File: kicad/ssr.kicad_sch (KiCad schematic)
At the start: 15 parts, among them J10 ULN spare, J11 SSR G17, J12 SSR G22, J13 SSR G23, J14 SSR G27, U4 ULN2803A

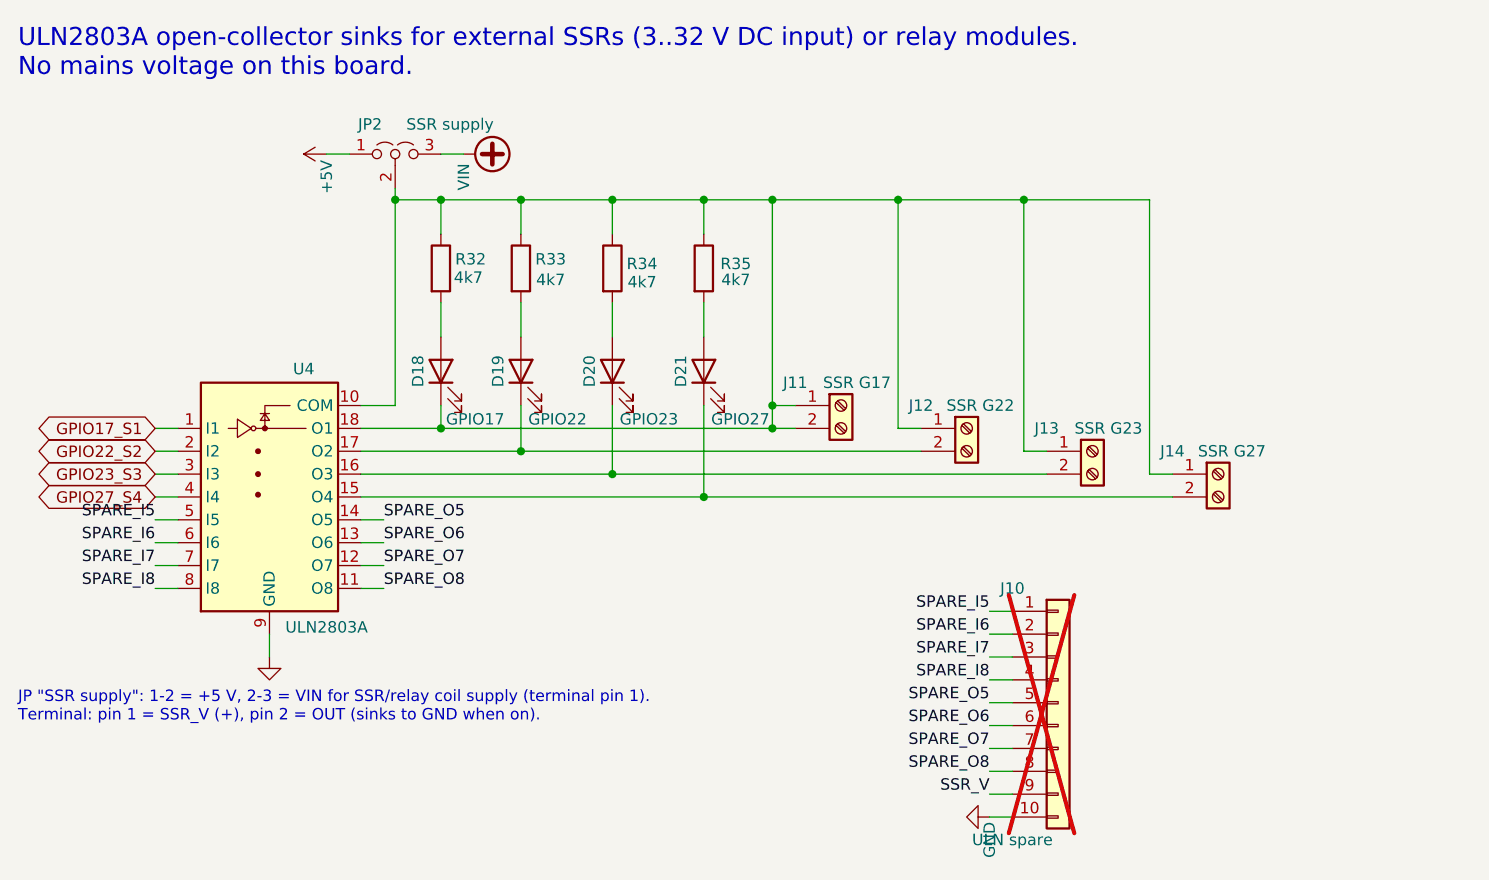
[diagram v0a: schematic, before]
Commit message: kicad: drop J10, fix S1 output shorted to SSR_V
- J10 (ULN2803 spare header) removed from schematic and board; the four
  unused ULN channels (U4 pins 5-8, 11-14) are marked no-connect
- schematic: a wire in front of J11 joined its two stubs, shorting the
  S1 output (U4 O1, D18, J11 pin 2) to SSR_V; removed. The board carried
  the merged net too but no copper joined both sides; pads and tracks
  are split again (SSR side now Net-(J11-Pin_1), S1 side Net-(D18-K))
- dangling 1.27 mm wire at R14 (outputs sheet) removed
ERC 0; DRC with schematic parity: only the known J2/Zero-hole overlap
and unrouted nets. Docs: J10 removed from README/BOM.

Co-Authored-By: Claude Opus 5.5 (1M context) <noreply@anthropic.com>
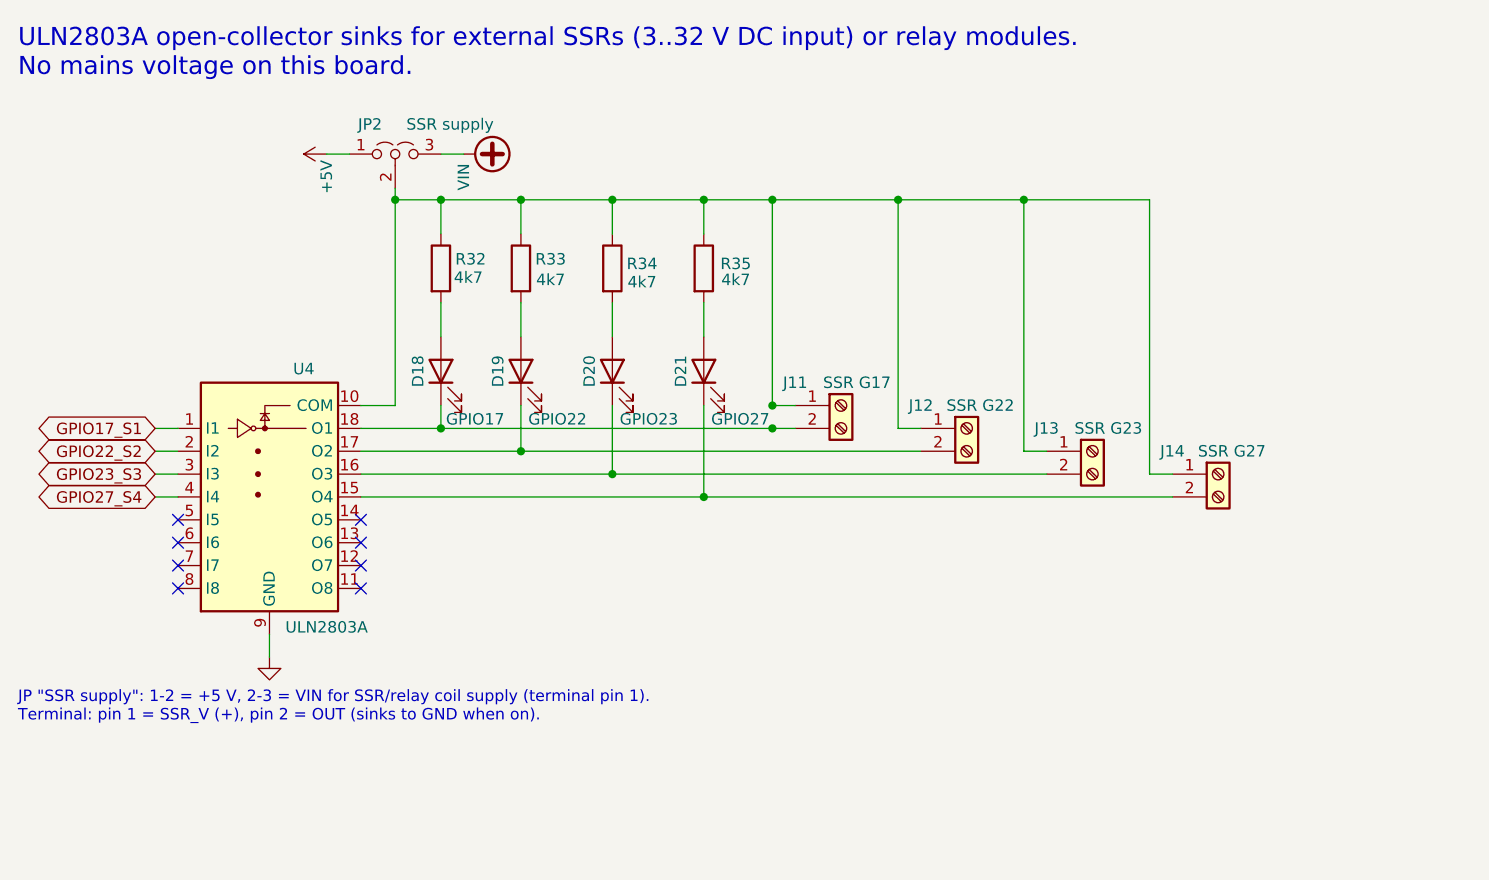
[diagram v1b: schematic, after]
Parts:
- removed J10: ULN spare, Connector_PinHeader_2.54mm:PinHeader_1x10_P2.54mm_Vertical, symbol Connector_Generic:Conn_01x10
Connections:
- net at J11.1 (Pin_1), J12.1 (Pin_1), J13.1 (Pin_1)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: no longer D18.1 (K), J11.2 (Pin_2), U4.18 (O1)
- net SPARE_I5: no longer names the net of U4.5 (I5)
- net SPARE_I6: no longer names the net of U4.6 (I6)
- net SPARE_I7: no longer names the net of U4.7 (I7)
- net SPARE_I8: no longer names the net of U4.8 (I8)
- net SPARE_O5: no longer names the net of U4.14 (O5)
- net SPARE_O6: no longer names the net of U4.13 (O6)
- net SPARE_O7: no longer names the net of U4.12 (O7)
- net SPARE_O8: no longer names the net of U4.11 (O8)
- new net: D18.1 (K), J11.2 (Pin_2), U4.18 (O1)
- no-connect marks 0 -> 8

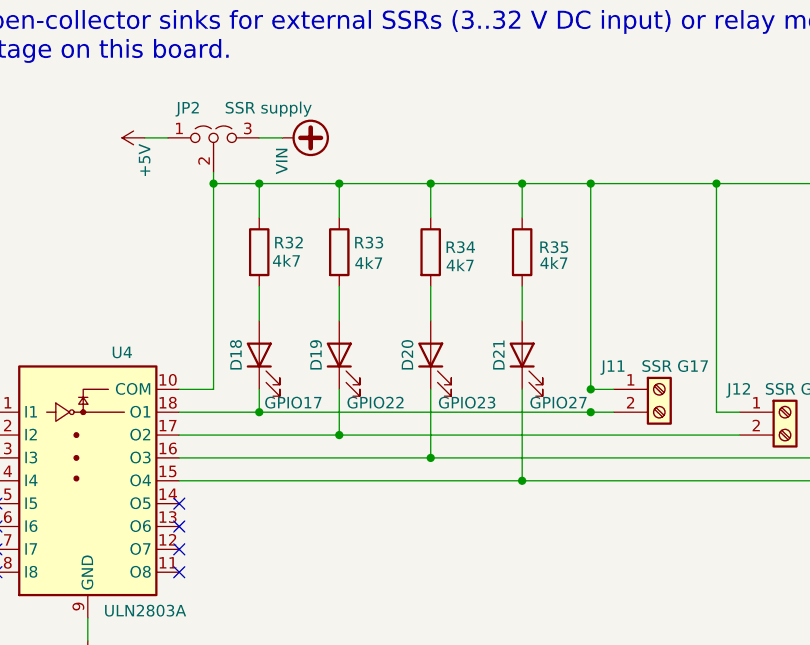
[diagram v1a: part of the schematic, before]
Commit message: kicad: restore net names lost while tidying the schematic
27 local labels re-added (Q1-Q6 _OUT/_G/_LED, S1-S4 _OUT/_LED, SSR_V);
the board nets are renamed with all pads and tracks. Connectivity is
unchanged, ERC 0, DRC with schematic parity clean. Q?_OUT match the
"Power" net class pattern again.

Co-Authored-By: Claude Opus 5.5 <noreply@anthropic.com>
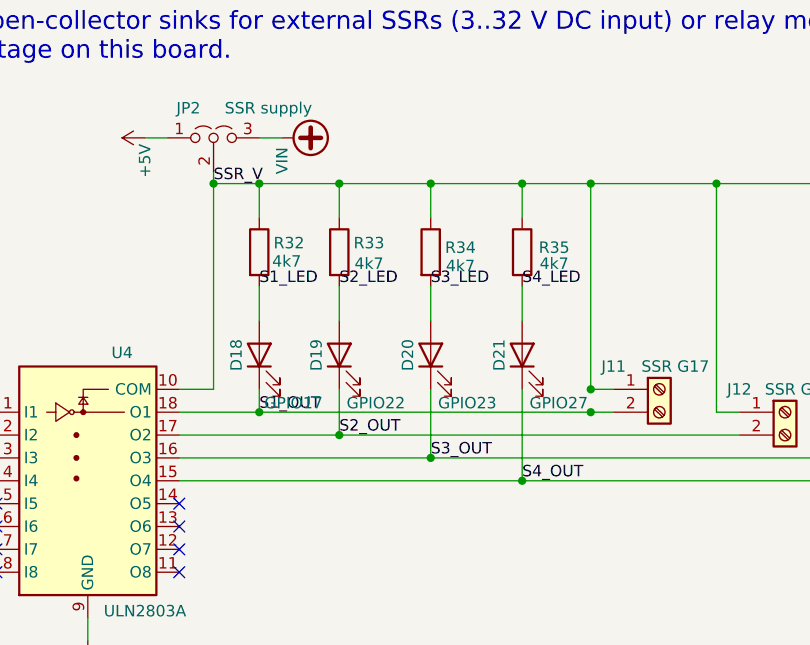
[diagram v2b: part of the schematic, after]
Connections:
- net SSR_V: now reaches J11.1 (Pin_1), J12.1 (Pin_1), J13.1 (Pin_1), J14.1 (Pin_1), JP2.2 (C), R32.1, R33.1, R34.1, R35.1, U4.10 (COM)
- net S4_LED: now reaches D21.2 (A), R35.2
- net S1_OUT: now reaches D18.1 (K), J11.2 (Pin_2), U4.18 (O1)
- net S3_OUT: now reaches D20.1 (K), J13.2 (Pin_2), U4.16 (O3)
- net S4_OUT: now reaches D21.1 (K), J14.2 (Pin_2), U4.15 (O4)
- net S1_LED: now reaches D18.2 (A), R32.2
- net S2_OUT: now reaches D19.1 (K), J12.2 (Pin_2), U4.17 (O2)
- net S2_LED: now reaches D19.2 (A), R33.2
- net S3_LED: now reaches D20.2 (A), R34.2
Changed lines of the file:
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@@
 		(at 63.5 92.71)
 	)
+	(label "S1_OUT"
+		(at 72.39 74.93 0)
+		(effects
+			(font
+				(size 1.27 1.27)
+			)
+			(justify left bottom)
+		)
+	)
+	(label "S1_LED"
+		(at 72.39 60.96 0)
+		(effects
+			(font
+				(size 1.27 1.27)
+			)
+			(justify left bottom)
+		)
+	)
+	(label "S2_OUT"
+		(at 81.28 77.47 0)
+		(effects
+			(font
+				(size 1.27 1.27)
+			)
+			(justify left bottom)
+		)
+	)
+	(label "S2_LED"
+		(at 81.28 60.96 0)
+		(effects
+			(font
+				(size 1.27 1.27)
+			)
+			(justify left bottom)
+		)
+	)
+	(label "S3_OUT"
+		(at 91.44 80.01 0)
+		(effects
+			(font
+				(size 1.27 1.27)
+			)
+			(justify left bottom)
+		)
+	)
+	(label "S3_LED"
+		(at 91.44 60.96 0)
+		(effects
+			(font
+				(size 1.27 1.27)
+			)
+			(justify left bottom)
+		)
+	)
+	(label "S4_OUT"
+		(at 101.6 82.55 0)
+		(effects
+			(font
+				(size 1.27 1.27)
+			)
+			(justify left bottom)
+		)
+	)
+	(label "S4_LED"
+		(at 101.6 60.96 0)
+		(effects
+			(font
+				(size 1.27 1.27)
+			)
+			(justify left bottom)
+		)
+	)
+	(label "SSR_V"
+		(at 67.31 49.53 0)
+		(effects
+			(font
+				(size 1.27 1.27)
+			)
+			(justify left bottom)
+		)
+	)
 )

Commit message: kicad: J1 polarity silk (+12V/GND), connector values match aquaPi port names
Terminal values now use the IoRegistry port names (PWM 0/1, GPIO n,
DS1820, ADC #1 in n) instead of the old "OUT G18"-style labels, several of
which were stale after the 74HCT244 reorder. Values stay on F.Fab; only the
J1 polarity marks are added to the silkscreen.

Co-Authored-By: Claude Opus 5.5 <noreply@anthropic.com>
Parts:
- J11: value SSR G17 -> GPIO 17
- J12: value SSR G22 -> GPIO 22
- J13: value SSR G23 -> GPIO 23
- J14: value SSR G27 -> GPIO 27
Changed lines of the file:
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@@
 			)
 		)
-		(property "Value" "SSR G17"
+		(property "Value" "GPIO 17"
 			(at 118.618 69.85 0)
 			(show_name no)
@@
 			)
 		)
-		(property "Value" "SSR G23"
+		(property "Value" "GPIO 23"
 			(at 146.558 74.93 0)
 			(show_name no)
@@
 			)
 		)
-		(property "Value" "SSR G27"
+		(property "Value" "GPIO 27"
 			(at 160.274 77.47 0)
 			(show_name no)
@@
 			)
 		)
-		(property "Value" "SSR G22"
+		(property "Value" "GPIO 22"
 			(at 132.334 72.39 0)
 			(show_name no)
